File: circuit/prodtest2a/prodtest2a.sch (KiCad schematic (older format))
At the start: 52 parts, among them J1 Conn_02x05_Odd_Even, J2 Conn_01x03, J3 Conn_02x05_Odd_Even, J4 Conn_01x05, J5 Conn_01x05, J6 Conn_Coaxial, Q1 IPP034N03L, SW1 SW_SPST, SW10 SW_SPST, SW11 SW_SPST, SW12 SW_SPST, SW13 SW_SPST, SW14 SW_SPST, SW15 SW_SPDT, SW16 SW_SPST, SW17 SW_SPST, SW18 SW_SPST, SW19 SW_SPST, SW2 SW_SPST, SW20 SW_SPST, SW21 SW_SPST, SW22 SW_SPST, SW23 SW_SPST, SW24 SW_SPST, SW3 SW_SPST, SW4 SW_SPST, SW5 SW_SPST, SW6 SW_SPST, SW7 SW_SPST, SW8 SW_SPST, SW9 SW_SPST, U1 MCP601-xP, U2 LM1084-ADJ

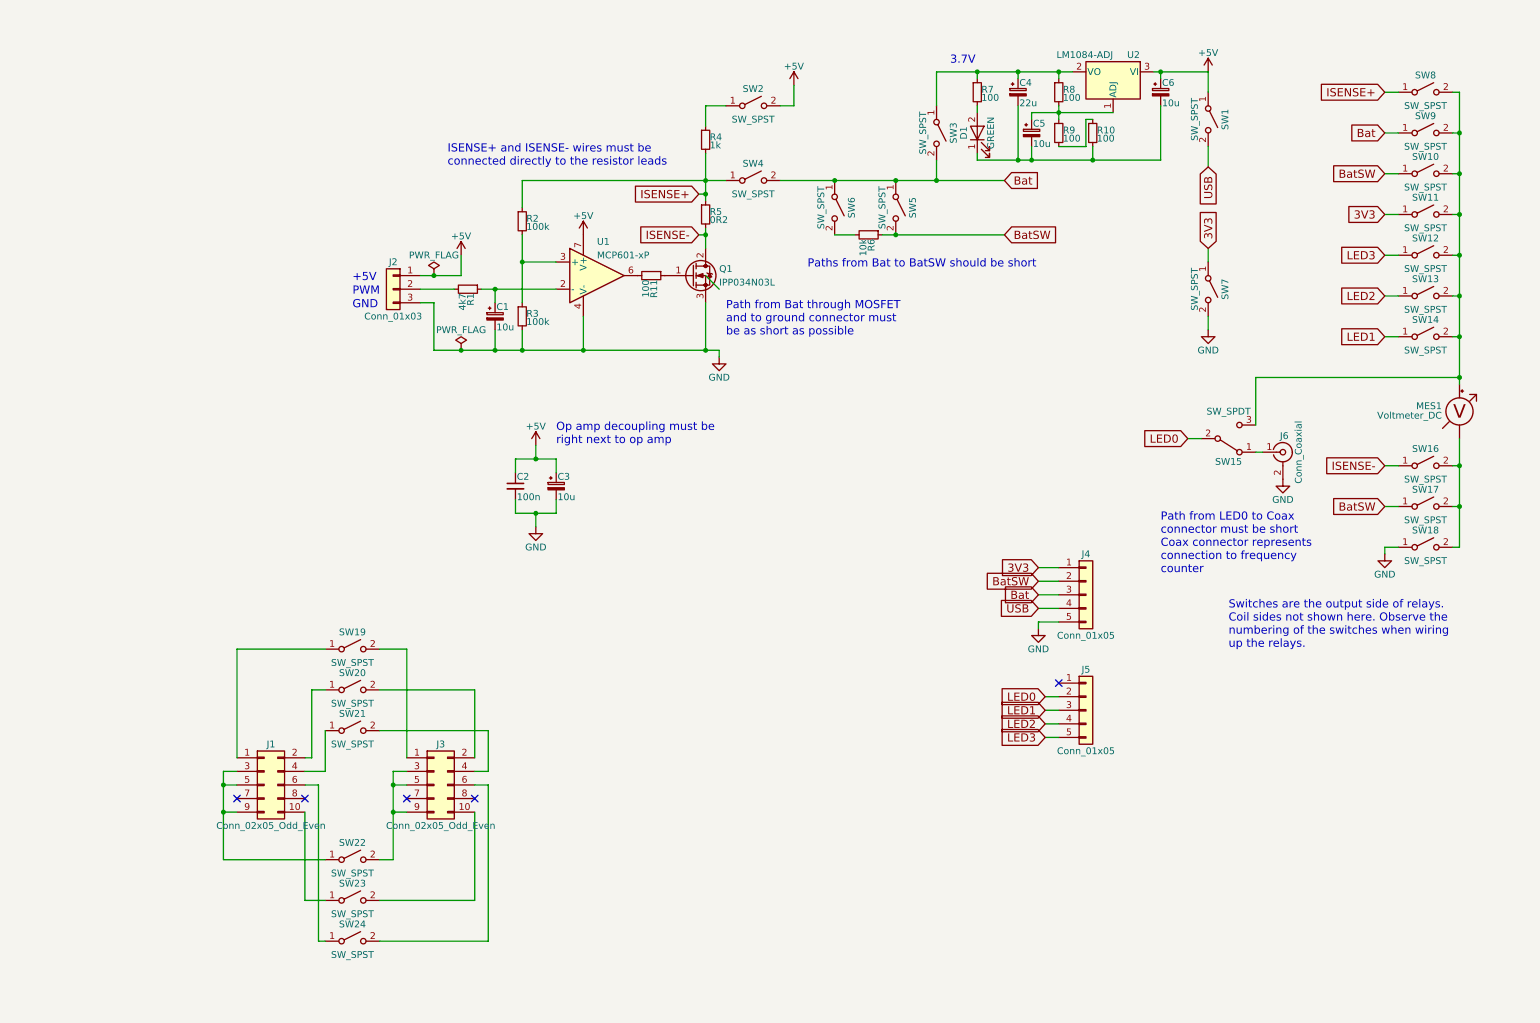
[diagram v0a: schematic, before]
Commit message: prodtest2a: design proper PCB
This integrates the relay functionality as well as the tester
onto a single PCB, designed to fit within an instrument enclosure.

Custom front and rear panels will need to be manufactured, probably
by 3D printing, to match this layout.

It is intended that the fixed test hardware will be connected to the
back panel, and that the DUT (via the jig) will be connected to the
front panel.

Signed-off-by: Gavan Fantom <gavan.fantom@unipart.io>
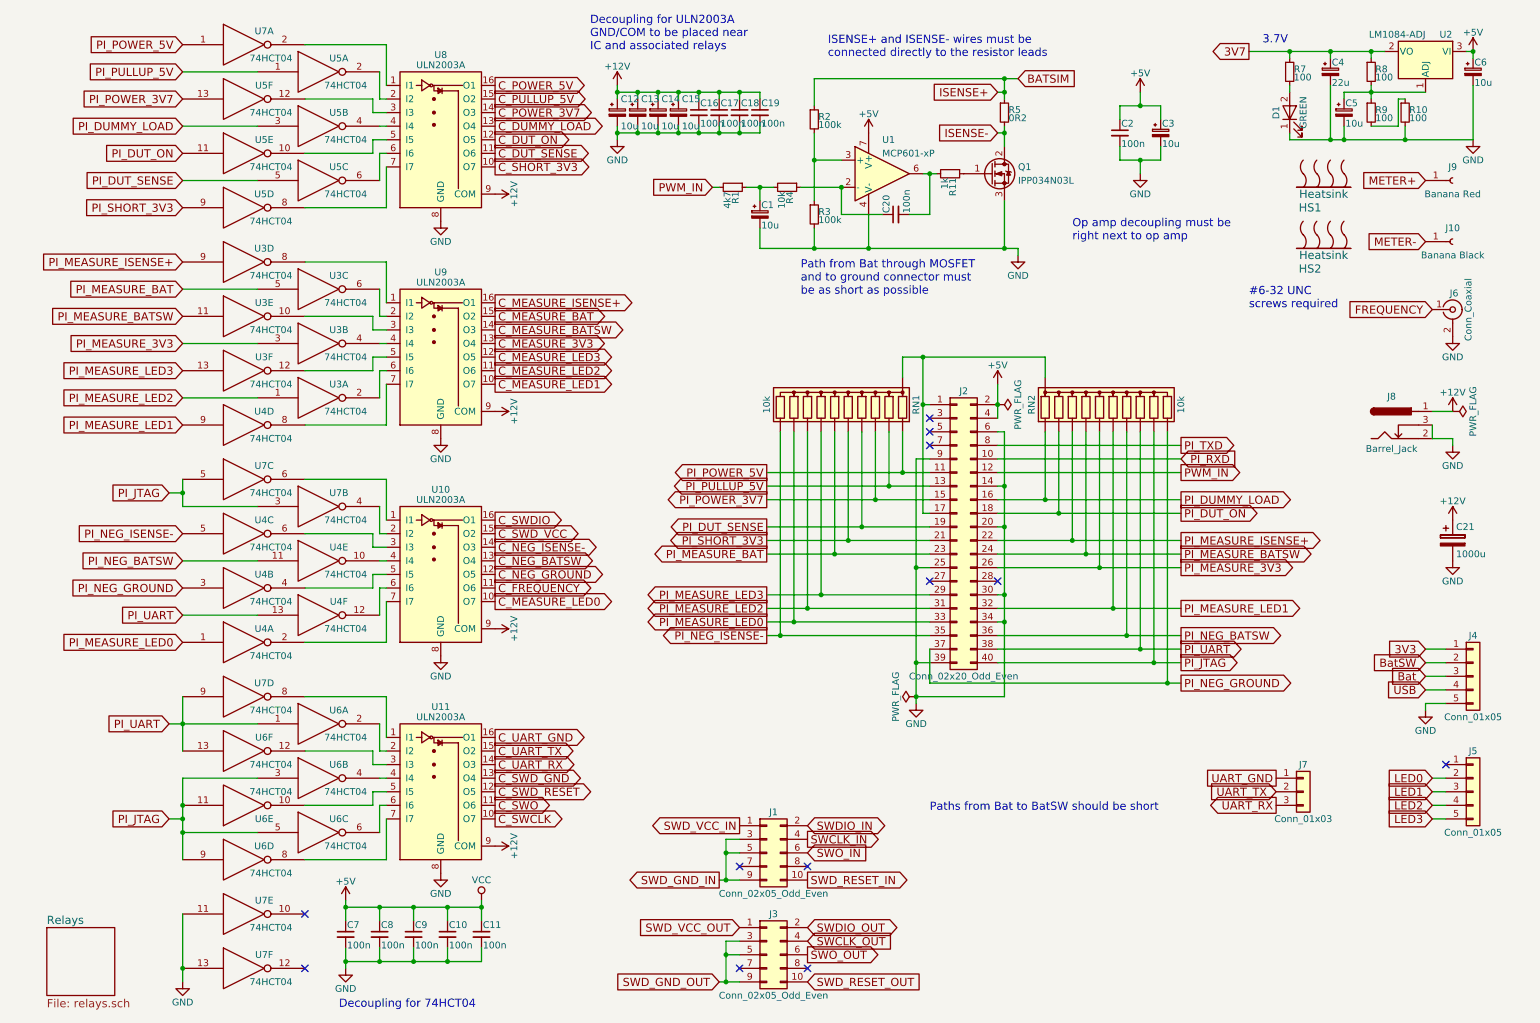
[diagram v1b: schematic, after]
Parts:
- removed J2: Conn_01x03, symbol Conn_01x03
- removed MES1: Voltmeter_DC, symbol Voltmeter_DC
- removed R6: 10k, symbol R_Small
- removed SW1, SW10, SW11, SW12, SW13, SW14, SW16, SW17, SW18, SW19, SW2, SW20, SW21, SW22, SW23, SW24, SW3, SW4, SW5, SW6, SW7, SW8, SW9: SW_SPST, symbol SW_SPST
- removed SW15: SW_SPDT, symbol SW_SPDT
- added C10, C11, C16, C17, C18, C19, C20, C7, C8, C9: 100n, Capacitors_THT:C_Disc_D5.0mm_W2.5mm_P5.00mm, symbol C_Small
- added C12, C13, C14, C15: 10u, Capacitors_THT:CP_Radial_D5.0mm_P2.00mm, symbol CP_Small
- added C21: 1000u, Capacitors_THT:CP_Radial_D10.0mm_P5.00mm, symbol CP
- added HS1, HS2: Heatsink, prodtest:Heatsink_Aavid_581002B02500G, symbol Heatsink
- added J10: Banana Black, prodtest:Staubli_4mm_Angled_Socket, symbol Conn_01x01_Female
- added J2: Conn_02x20_Odd_Even, Pin_Headers:Pin_Header_Angled_2x20_Pitch2.54mm, symbol Conn_02x20_Odd_Even
- added J7: Conn_01x03, Pin_Headers:Pin_Header_Angled_1x03_Pitch2.54mm, symbol Conn_01x03
- added J8: Barrel_Jack, Connectors:BARREL_JACK, symbol Barrel_Jack
- added J9: Banana Red, prodtest:Staubli_4mm_Angled_Socket, symbol Conn_01x01_Female
- added RN1, RN2: 10k, Resistors_THT:R_Array_SIP11, symbol R_Network10
- added U10, U11, U8, U9: ULN2003A, Housings_DIP:DIP-16_W7.62mm, symbol ULN2003A
- added U3, U4, U5, U6, U7: 74HCT04, Housings_DIP:DIP-14_W7.62mm, symbol 74HCT04
- C1, C3, C5, C6: footprint (none) -> Capacitors_THT:CP_Radial_D5.0mm_P2.00mm; SPURL (none) -> -
- C2: footprint (none) -> Capacitors_THT:C_Disc_D5.0mm_W2.5mm_P5.00mm; SPURL (none) -> -
- C4: footprint (none) -> Capacitors_THT:CP_Radial_Tantal_D6.0mm_P5.00mm; SPURL (none) -> -
- D1: footprint (none) -> prodtest:LED_D3.0mm_Horizontal_Housing_Z5.0mm; MPN L-1503GD -> L-710A8EW/1GD; SPN 2335726 -> 2001694; SPURL (none) -> -
- J1, J3: footprint (none) -> Pin_Headers:Pin_Header_Angled_2x05_Pitch1.27mm; MFR (none) -> Samtec; MPN (none) -> FTSH-105-01-L-D-RA-K; SPN (none) -> 2856878; SPR (none) -> Farnell; SPURL (none) -> -
- J4, J5: footprint (none) -> Pin_Headers:Pin_Header_Angled_1x05_Pitch2.54mm; MFR (none) -> Wurth; MPN (none) -> 61300511021; SPN (none) -> 2356179; SPR (none) -> Farnell; SPURL (none) -> -
- J6: footprint (none) -> prodtest:BNC_Elbow_Socket_TE_1-1337543-0; MFR Pomona -> Greenpar; MPN 4969 -> 1-1337543-0; SPN 4435710 -> 1020955; SPURL (none) -> -
- Q1, U2: footprint (none) -> TO_SOT_Packages_THT:TO-220-3_Vertical; SPURL (none) -> -
- R1, R10, R2, R3, R7, R8, R9: footprint (none) -> Resistors_THT:R_Axial_DIN0204_L3.6mm_D1.6mm_P5.08mm_Horizontal; SPURL (none) -> -
- R11: value 100 -> 1k; footprint (none) -> Resistors_THT:R_Axial_DIN0204_L3.6mm_D1.6mm_P5.08mm_Horizontal; MPN MF12 100R -> MF12 1K; SPN 9342397 -> 9342400; SPURL (none) -> -
- R4: value 1k -> 10k; footprint (none) -> Resistors_THT:R_Axial_DIN0204_L3.6mm_D1.6mm_P5.08mm_Horizontal; MPN MF12 1K -> MF12 10K; SPN 9342400 -> 9342419; SPURL (none) -> -
- R5: footprint (none) -> Resistors_THT:R_Axial_Power_L20.0mm_W6.4mm_P22.40mm; SPURL (none) -> -
- U1: footprint (none) -> Housings_DIP:DIP-8_W7.62mm; SPURL (none) -> -
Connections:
- net +5V: now also C10.1, C11.1, C7.1, C8.1, C9.1, J2.2 (Pin_2), J2.4 (Pin_4), U3.14 (VCC), U3.14 (VCC), U3.14 (VCC), U3.14 (VCC), U3.14 (VCC), U3.14 (VCC), U4.14 (VCC), U4.14 (VCC), U4.14 (VCC), U4.14 (VCC), U4.14 (VCC), U4.14 (VCC), U5.14 (VCC), U5.14 (VCC), U5.14 (VCC), U5.14 (VCC), U5.14 (VCC), U5.14 (VCC), U6.14 (VCC), U6.14 (VCC), U6.14 (VCC), U6.14 (VCC), U6.14 (VCC), U6.14 (VCC), U7.14 (VCC), U7.14 (VCC), U7.14 (VCC), U7.14 (VCC), U7.14 (VCC), U7.14 (VCC)
- net GND: now also C4.2, C5.2, C6.2, D1.1 (K), R10.2, C10.2, C11.2, C12.2, C13.2, C14.2, C15.2, C16.2, C17.2, C18.2, C19.2, C21.2, C7.2, C8.2, C9.2, J2.14 (Pin_14), J2.20 (Pin_20), J2.25 (Pin_25), J2.30 (Pin_30), J2.34 (Pin_34), J2.39 (Pin_39), J2.6 (Pin_6), J2.9 (Pin_9), J8.2, J8.3, U10.8 (GND), U11.8 (GND), U3.7 (GND), U3.7 (GND), U3.7 (GND), U3.7 (GND), U3.7 (GND), U3.7 (GND), U4.7 (GND), U4.7 (GND), U4.7 (GND), U4.7 (GND), U4.7 (GND), U4.7 (GND), U5.7 (GND), U5.7 (GND), U5.7 (GND), U5.7 (GND), U5.7 (GND), U5.7 (GND), U6.7 (GND), U6.7 (GND), U6.7 (GND), U6.7 (GND), U6.7 (GND), U6.7 (GND), U7.11, U7.13, U7.7 (GND), U7.7 (GND), U7.7 (GND), U7.7 (GND), U7.7 (GND), U7.7 (GND), U8.8 (GND), U9.8 (GND)
- net 3V7: now reaches C4.1, R7.1, R8.1, U2.2 (VO)
- net at C1.1, R1.1: now also R4.2; no longer U1.2 (-)
- net at R11.2, U1.6: now also C20.2
- net PWM_IN: now reaches R1.2
- net PWM_IN: now also J2.12 (Pin_12)
- net at R4.1: now also U1.2 (-), C20.1
- net FREQUENCY: now reaches J6.1 (In)
- net SWD_VCC_IN: now reaches J1.1 (Pin_1)
- net SWD_RESET_IN: now reaches J1.10 (Pin_10)
- net SWDIO_IN: now reaches J1.2 (Pin_2)
- net SWD_GND_IN: now reaches J1.3 (Pin_3), J1.5 (Pin_5), J1.9 (Pin_9)
- net SWCLK_IN: now reaches J1.4 (Pin_4)
- net SWO_IN: now reaches J1.6 (Pin_6)
- net SWD_VCC_OUT: now reaches J3.1 (Pin_1)
- net SWD_RESET_OUT: now reaches J3.10 (Pin_10)
- net SWDIO_OUT: now reaches J3.2 (Pin_2)
- net SWD_GND_OUT: now reaches J3.3 (Pin_3), J3.5 (Pin_5), J3.9 (Pin_9)
- net SWCLK_OUT: now reaches J3.4 (Pin_4)
- net SWO_OUT: now reaches J3.6 (Pin_6)
- net ISENSE+ renamed BATSIM
- net BATSIM: no longer R4.2
- new net: U7.2, U8.1 (I1)
- new net: U5.2, U8.2 (I2)
- new net: U5.12, U8.3 (I3)
- new net: U5.4, U8.4 (I4)
- new net: U5.10, U8.5 (I5)
- new net: U5.6, U8.6 (I6)
- new net: U5.8, U8.7 (I7)
- new net: J2.1 (Pin_1), J2.17 (Pin_17), RN1.1 (common), RN2.1 (common)
- new net: U3.8, U9.1 (I1)
- new net: U3.6, U9.2 (I2)
- new net: U3.10, U9.3 (I3)
- new net: U3.4, U9.4 (I4)
- new net: U3.12, U9.5 (I5)
- new net: U3.2, U9.6 (I6)
- new net: U4.8, U9.7 (I7)
- new net: U10.1 (I1), U7.6
- new net: U10.2 (I2), U7.4
- new net: U10.3 (I3), U4.6
- new net: U10.4 (I4), U4.10
- new net: U10.5 (I5), U4.4
- new net: U10.6 (I6), U4.12
- new net: U10.7 (I7), U4.2
- new net: U11.1 (I1), U7.8
- new net: U11.2 (I2), U6.2
- new net: U11.3 (I3), U6.12
- new net: U11.4 (I4), U6.4
- new net: U11.5 (I5), U6.10
- new net: U11.6 (I6), U6.6
- new net: U11.7 (I7), U6.8
- new net +12V: C12.1, C13.1, C14.1, C15.1, C16.1, C17.1, C18.1, C19.1, C21.1, J8.1, U10.9 (COM), U11.9 (COM), U8.9 (COM), U9.9 (COM)
- new net C_DUMMY_LOAD: U8.13 (O4)
- new net C_DUT_ON: U8.12 (O5)
- new net C_DUT_SENSE: U8.11 (O6)
- new net C_FREQUENCY: U10.11 (O6)
- new net C_MEASURE_3V3: U9.13 (O4)
- new net C_MEASURE_BAT: U9.15 (O2)
- new net C_MEASURE_BATSW: U9.14 (O3)
- new net C_MEASURE_ISENSE+: U9.16 (O1)
- new net C_MEASURE_LED0: U10.10 (O7)
- new net C_MEASURE_LED1: U9.10 (O7)
- new net C_MEASURE_LED2: U9.11 (O6)
- new net C_MEASURE_LED3: U9.12 (O5)
- new net C_NEG_BATSW: U10.13 (O4)
- new net C_NEG_GROUND: U10.12 (O5)
- new net C_NEG_ISENSE-: U10.14 (O3)
- new net C_POWER_3V7: U8.14 (O3)
- new net C_POWER_5V: U8.16 (O1)
- new net C_PULLUP_5V: U8.15 (O2)
- new net C_SHORT_3V3: U8.10 (O7)
- new net C_SWCLK: U11.10 (O7)
- new net C_SWDIO: U10.16 (O1)
- new net C_SWD_GND: U11.13 (O4)
- new net C_SWD_RESET: U11.12 (O5)
- new net C_SWD_VCC: U10.15 (O2)
- new net C_SWO: U11.11 (O6)
- new net C_UART_GND: U11.16 (O1)
- new net C_UART_RX: U11.14 (O3)
- new net C_UART_TX: U11.15 (O2)
- new net METER+: J9.1 (Pin_1)
- new net METER-: J10.1 (Pin_1)
- new net PI_DUMMY_LOAD: J2.16 (Pin_16), RN2.2 (R1), U5.3
- new net PI_DUT_ON: J2.18 (Pin_18), RN2.3 (R2), U5.11
- new net PI_DUT_SENSE: J2.19 (Pin_19), RN1.5 (R4), U5.5
- new net PI_JTAG: J2.40 (Pin_40), RN2.10 (R9), U6.11, U6.3, U6.5, U6.9, U7.3, U7.5
- new net PI_MEASURE_3V3: J2.26 (Pin_26), RN2.6 (R5), U3.3
- new net PI_MEASURE_BAT: J2.23 (Pin_23), RN1.7 (R6), U3.5
- new net PI_MEASURE_BATSW: J2.24 (Pin_24), RN2.5 (R4), U3.11
- new net PI_MEASURE_ISENSE+: J2.22 (Pin_22), RN2.4 (R3), U3.9
- new net PI_MEASURE_LED0: J2.33 (Pin_33), RN1.10 (R9), U4.1
- new net PI_MEASURE_LED1: J2.32 (Pin_32), RN2.7 (R6), U4.9
- new net PI_MEASURE_LED2: J2.31 (Pin_31), RN1.9 (R8), U3.1
- new net PI_MEASURE_LED3: J2.29 (Pin_29), RN1.8 (R7), U3.13
- new net PI_NEG_BATSW: J2.36 (Pin_36), RN2.8 (R7), U4.11
- new net PI_NEG_GROUND: J2.37 (Pin_37), RN2.11 (R10), U4.3
- new net PI_NEG_ISENSE-: J2.35 (Pin_35), RN1.11 (R10), U4.5
- new net PI_POWER_3V7: J2.15 (Pin_15), RN1.4 (R3), U5.13
- new net PI_POWER_5V: J2.11 (Pin_11), RN1.2 (R1), U7.1
- new net PI_PULLUP_5V: J2.13 (Pin_13), RN1.3 (R2), U5.1
- new net PI_RXD: J2.10 (Pin_10)
- new net PI_SHORT_3V3: J2.21 (Pin_21), RN1.6 (R5), U5.9
- new net PI_TXD: J2.8 (Pin_8)
- new net PI_UART: J2.38 (Pin_38), RN2.9 (R8), U4.13, U6.1, U6.13, U7.9
- new net UART_GND: J7.1 (Pin_1)
- new net UART_RX: J7.3 (Pin_3)
- new net UART_TX: J7.2 (Pin_2)
- no-connect marks 5 -> 12
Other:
- note added: "#6-32 UNC\nscrews required"
- note added: "Decoupling for 74HCT04"
- note added: "Decoupling for ULN2003A\nGND/COM to be placed near\nIC and associated relays"
- note removed: "+5V"
- note removed: "GND"
- note removed: "PWM"
- note removed: "Path from LED0 to Coax\nconnector must be short\nCoax connector represents\nconnection to frequency\ncounter"
- note removed: "Switches are the output side of relays.\nCoil sides not shown here. Observe the\nnumbering of the switches when wiring\nup the relays."
- moved on the sheet: C1, C2, C3, C4, C5, C6, D1, J1, J4, J6, Q1, R1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
